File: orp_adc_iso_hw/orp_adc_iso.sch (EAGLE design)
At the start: 19 parts, among them IC1 AD8603AUJZ-REEL7, IC2 LM385MX-2.5_NOPB, IC3 ADS1115IDGSR, IC4 ADUM1250ARZ, J1 RF1-01B-D-00-75

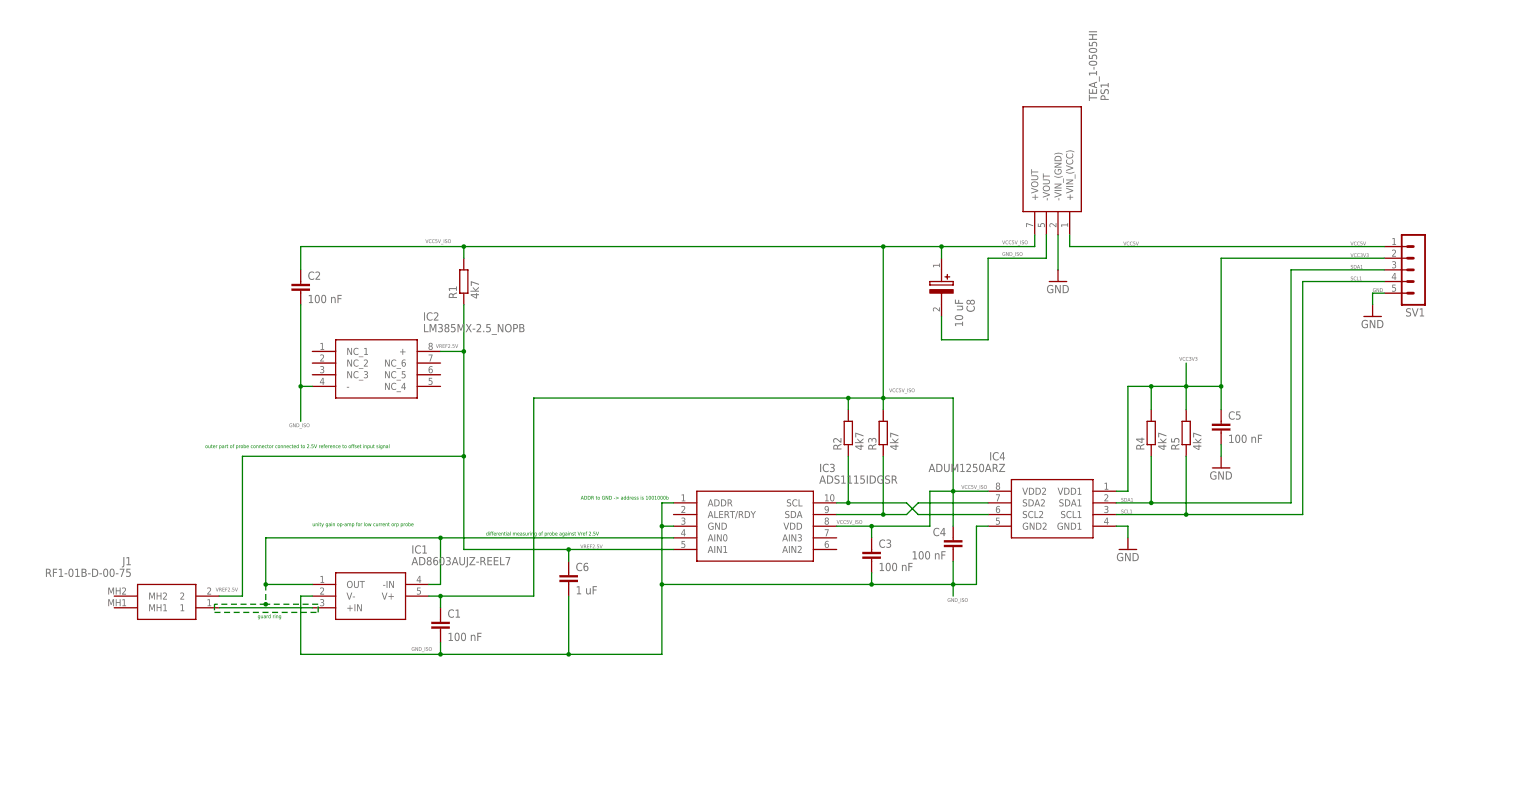
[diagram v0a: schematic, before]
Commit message: schema cleanup, added capacitors
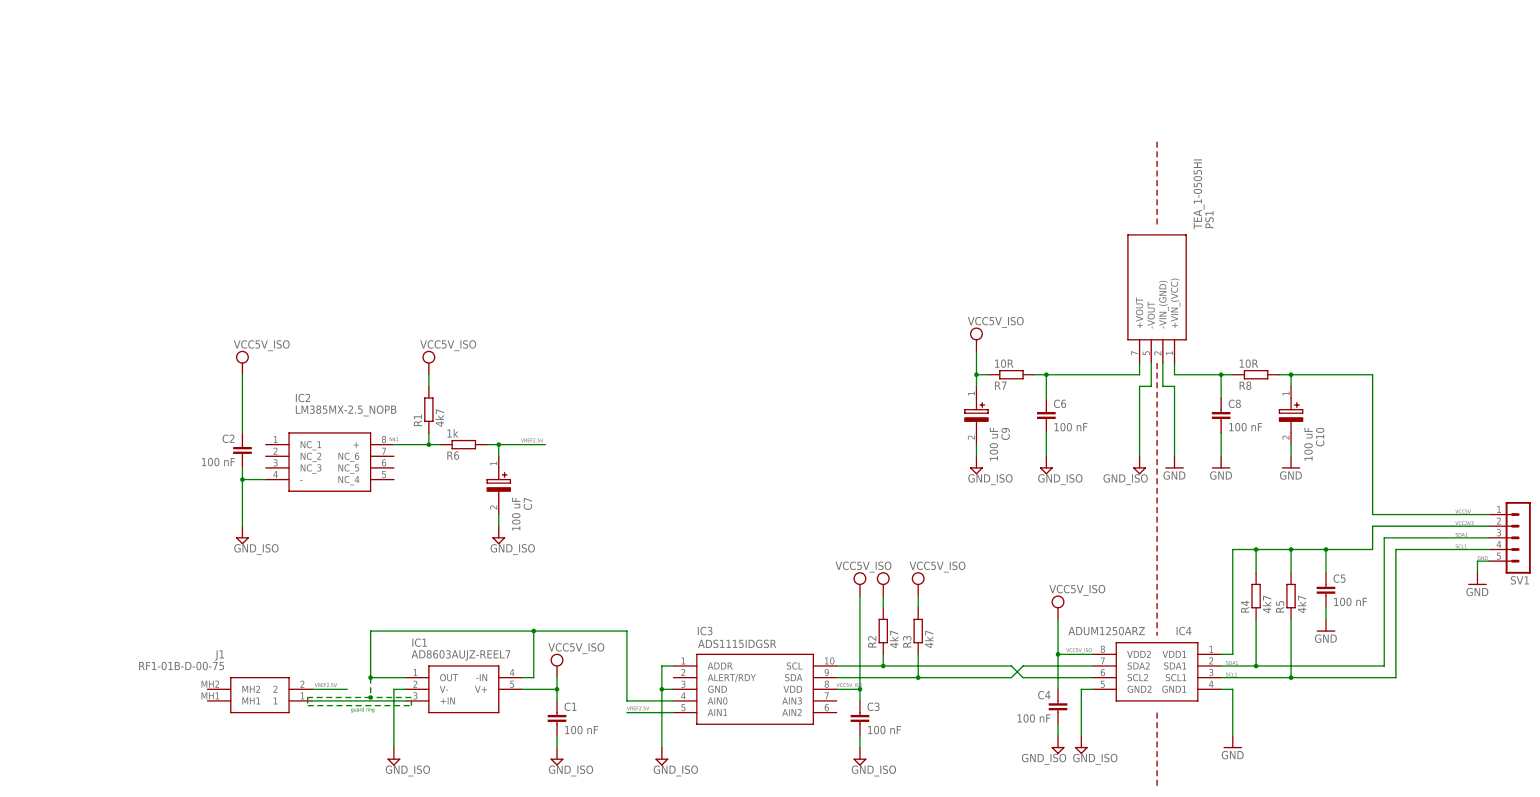
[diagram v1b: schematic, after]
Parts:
- added C10, C7, C9: 100 uF, 293D106X9016B2TE3:293D106X9016B2TE3
- added R6: 1k, rcl:R-EU_R0603
- added R7, R8: 10R, rcl:R-EU_R0603
- C6: value 1 uF -> 100 nF; device rcl:C-EUC0805 -> rcl:C-EUC0603
- C8: value 10 uF -> 100 nF; device 293D106X9016B2TE3:293D106X9016B2TE3 -> rcl:C-EUC0603
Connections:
- new net N$1: IC2.+, R1.1, R6.1
- new net VCC5V_INTERNAL: C8.1, PS1.+VIN_(VCC), R8.1
- new net VCC5V_ISO_INTERNAL: C6.1, PS1.+VOUT, R7.2
- net GND: now also C10.-, C8.2
- net GND_ISO: now also C7.-, C9.-; no longer C8.-
- net VCC5V: now also C10.+, R8.2; no longer PS1.+VIN_(VCC)
- net VCC5V_ISO: now also C9.+, R7.1; no longer C8.+, PS1.+VOUT
- net VREF2.5V: now also C7.+, R6.2; no longer C6.1, IC2.+, R1.1
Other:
- note removed: "ADDR to GND -> address is 1001000b"
- note removed: "differential measuring of probe against Vref 2.5V"
- note removed: "outer part of probe connector connected to 2.5V reference to offset input signal"
- note removed: "unity gain op-amp for low current orp probe"
- moved on the sheet: C1, C2, C3, C4, C5, C6, IC1, IC2, IC3, IC4, J1, PS1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
